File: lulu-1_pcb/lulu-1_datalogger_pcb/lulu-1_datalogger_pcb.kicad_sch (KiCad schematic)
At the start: 31 parts, among them J1 SD_Card_Receptacle, J3 USB_C_Receptacle_USB2.0_16P, J4 Conn_01x20_Socket, J5 Screw_Terminal_01x03, SW1 SW_Nidec_CAS-120A1, U1 STM32F401RETx, U2 BMP280, U3 MPU-6050, U4 W25Q16JVSS, U5 BD33FC0FP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

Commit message: deleted project
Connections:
- net GND: now also SW1.3 (A); no longer SW1.2 (B)
- net at R5.1: now also SW1.2 (B); no longer SW1.3 (A)
- no-connect marks 53 -> 51
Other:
- moved on the sheet: R5, SW1
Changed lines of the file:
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@@
 	)
 	(no_connect
-		(at 264.16 26.67)
-	)
-	(no_connect
 		(at 168.91 134.62)
 	)
@@
 	)
 	(no_connect
-		(at 218.44 39.37)
-	)
-	(no_connect
 		(at 168.91 129.54)
 	)
@@
 	(wire
 		(pts
+			(xy 113.03 60.96) (xy 115.57 60.96)
+		)
+		(stroke
+			(width 0)
+			(type default)
+		)
+	)
+	(wire
+		(pts
 			(xy 254 29.21) (xy 254 30.48)
 		)
@@
 	(wire
 		(pts
-			(xy 111.76 67.31) (xy 111.76 66.04)
-		)
-		(stroke
-			(width 0)
-			(type default)
-		)
-	)
-	(wire
-		(pts
 			(xy 254 91.44) (xy 250.19 91.44)
 		)
@@
 	(wire
 		(pts
+			(xy 254 26.67) (xy 264.16 26.67)
+		)
+		(stroke
+			(width 0)
+			(type default)
+		)
+	)
+	(wire
+		(pts
 			(xy 209.55 46.99) (xy 209.55 49.53)
 		)
@@
 	(wire
 		(pts
+			(xy 133.35 63.5) (xy 135.89 63.5)
+		)
+		(stroke
+			(width 0)
+			(type default)
+		)
+	)
+	(wire
+		(pts
 			(xy 43.18 90.17) (xy 45.72 90.17)
 		)
@@
 	(wire
 		(pts
-			(xy 125.73 68.58) (xy 123.19 68.58)
-		)
-		(stroke
-			(width 0)
-			(type default)
-		)
-	)
-	(wire
-		(pts
 			(xy 104.14 76.2) (xy 104.14 78.74)
 		)
@@
 	(wire
 		(pts
+			(xy 111.76 66.04) (xy 115.57 66.04)
+		)
+		(stroke
+			(width 0)
+			(type default)
+		)
+	)
+	(wire
+		(pts
 			(xy 78.74 119.38) (xy 82.55 119.38)
 		)
@@
 	(wire
 		(pts
-			(xy 135.89 63.5) (xy 130.81 63.5)
+			(xy 43.18 80.01) (xy 46.99 80.01)
 		)
 		(stroke
@@
 	(wire
 		(pts
-			(xy 43.18 80.01) (xy 46.99 80.01)
+			(xy 212.09 39.37) (xy 218.44 39.37)
 		)
 		(stroke
@@
 	(wire
 		(pts
-			(xy 111.76 66.04) (xy 113.03 66.04)
-		)
-		(stroke
-			(width 0)
-			(type default)
-		)
-	)
-	(wire
-		(pts
 			(xy 264.16 31.75) (xy 256.54 31.75)
 		)
@@
 	(symbol
 		(lib_id "Switch:SW_Nidec_CAS-120A1")
-		(at 118.11 66.04 0)
+		(at 120.65 63.5 180)
 		(unit 1)
 		(exclude_from_sim no)
@@
 		(on_board yes)
 		(dnp no)
-		(fields_autoplaced yes)
 		(property "Reference" "SW1"
-			(at 118.11 59.69 0)
+			(at 120.396 58.674 0)
 			(effects
 				(font
@@
 		)
 		(property "Value" "SW_Nidec_CAS-120A1"
-			(at 118.11 59.69 0)
+			(at 120.65 69.85 0)
 			(effects
 				(font
@@
 		)
 		(property "Footprint" "Button_Switch_SMD:Nidec_Copal_CAS-120A"
-			(at 118.11 76.2 0)
+			(at 120.65 53.34 0)
 			(effects
 				(font
@@
 		)
 		(property "Datasheet" "https://www.nidec-components.com/e/catalog/switch/cas.pdf"
-			(at 118.11 73.66 0)
+			(at 120.65 55.88 0)
 			(effects
 				(font
@@
 		)
 		(property "Description" "Switch, single pole double throw"
-			(at 118.11 66.04 0)
+			(at 120.65 63.5 0)
 			(effects
 				(font
@@
 	(symbol
 		(lib_id "Device:R")
-		(at 127 63.5 90)
+		(at 129.54 63.5 90)
 		(unit 1)
 		(exclude_from_sim no)
@@
 		(dnp no)
 		(property "Reference" "R5"
-			(at 126.492 58.928 90)
+			(at 129.032 58.928 90)
 			(effects
 				(font
@@
 		)
 		(property "Value" "10k"
-			(at 126.746 61.214 90)
+			(at 129.286 61.214 90)
 			(effects
 				(font
@@
 		)
 		(property "Footprint" ""
-			(at 127 65.278 90)
+			(at 129.54 65.278 90)
 			(effects
 				(font
@@
 		)
 		(property "Datasheet" "~"
-			(at 127 63.5 0)
+			(at 129.54 63.5 0)
 			(effects
 				(font
@@
 		)
 		(property "Description" "Resistor"
-			(at 127 63.5 0)
+			(at 129.54 63.5 0)
 			(effects
 				(font
@@
 	(symbol
 		(lib_id "power:VDD")
-		(at 125.73 68.58 270)
+		(at 113.03 60.96 90)
 		(unit 1)
 		(exclude_from_sim no)
@@
 		(dnp no)
 		(property "Reference" "#PWR018"
-			(at 121.92 68.58 0)
+			(at 116.84 60.96 0)
 			(effects
 				(font
@@
 		)
 		(property "Value" "+3.3V"
-			(at 126.492 71.12 90)
+			(at 115.57 58.928 90)
 			(effects
 				(font
@@
 		)
 		(property "Footprint" ""
-			(at 125.73 68.58 0)
+			(at 113.03 60.96 0)
 			(effects
 				(font
@@
 		)
 		(property "Datasheet" ""
-			(at 125.73 68.58 0)
+			(at 113.03 60.96 0)
 			(effects
 				(font
@@
 		)
 		(property "Description" "Power symbol creates a global label with name \"VDD\""
-			(at 125.73 68.58 0)
+			(at 113.03 60.96 0)
 			(effects
 				(font
@@
 	(symbol
 		(lib_id "power:GND")
-		(at 111.76 67.31 0)
+		(at 111.76 66.04 0)
 		(unit 1)
 		(exclude_from_sim no)
@@
 		(dnp no)
 		(property "Reference" "#PWR019"
-			(at 111.76 73.66 0)
+			(at 111.76 72.39 0)
 			(effects
 				(font
@@
 		)
 		(property "Value" "GND"
-			(at 111.76 71.12 0)
+			(at 111.76 69.85 0)
 			(effects
 				(font
@@
 		)
 		(property "Footprint" ""
-			(at 111.76 67.31 0)
+			(at 111.76 66.04 0)
 			(effects
 				(font
@@
 		)
 		(property "Datasheet" ""
-			(at 111.76 67.31 0)
+			(at 111.76 66.04 0)
 			(effects
 				(font
@@
 		)
 		(property "Description" "Power symbol creates a global label with name \"GND\" , ground"
-			(at 111.76 67.31 0)
+			(at 111.76 66.04 0)
 			(effects
 				(font

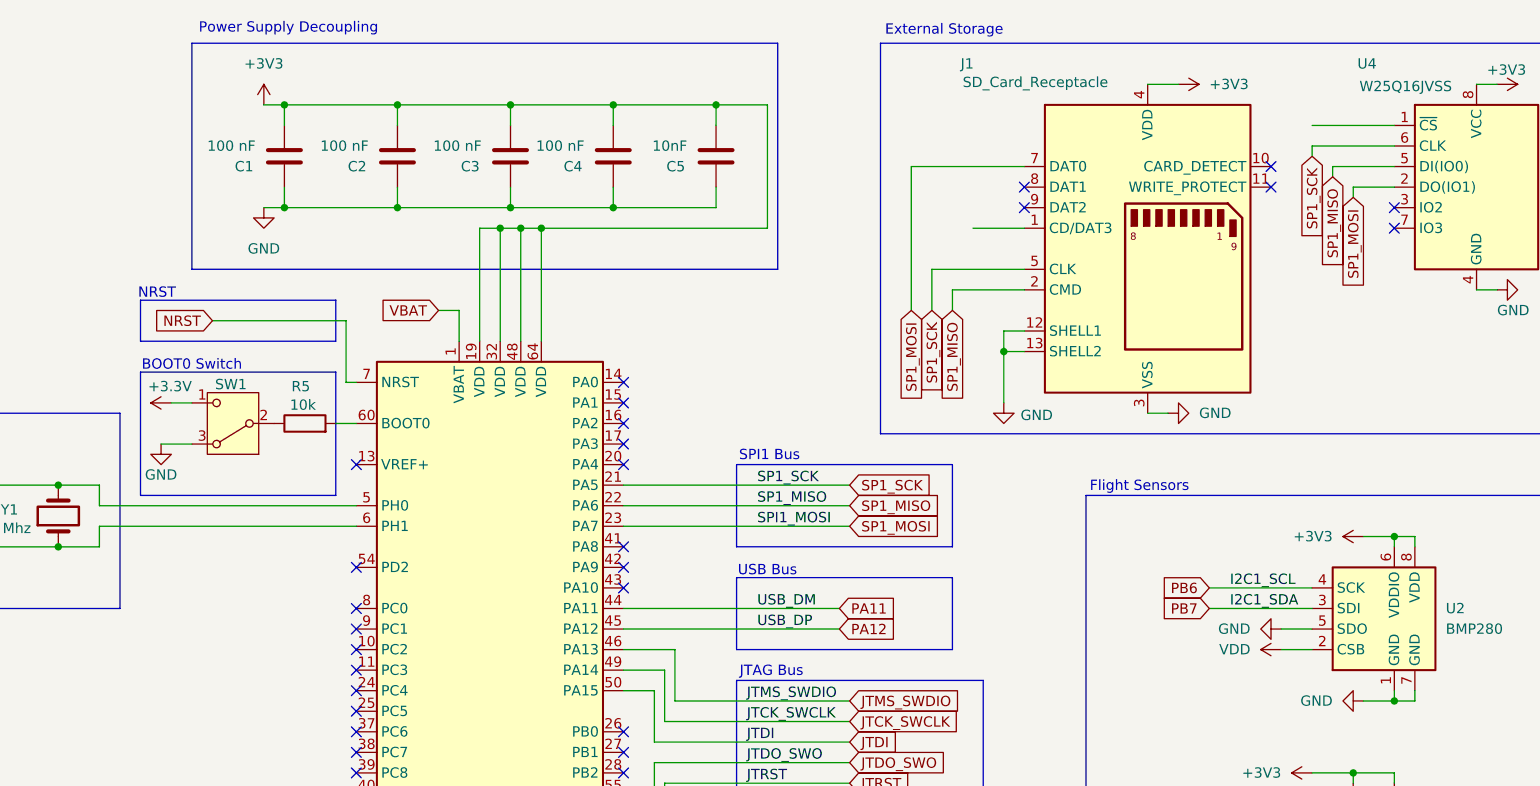
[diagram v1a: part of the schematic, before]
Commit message: initialised pins for SPI CS and added on schematic
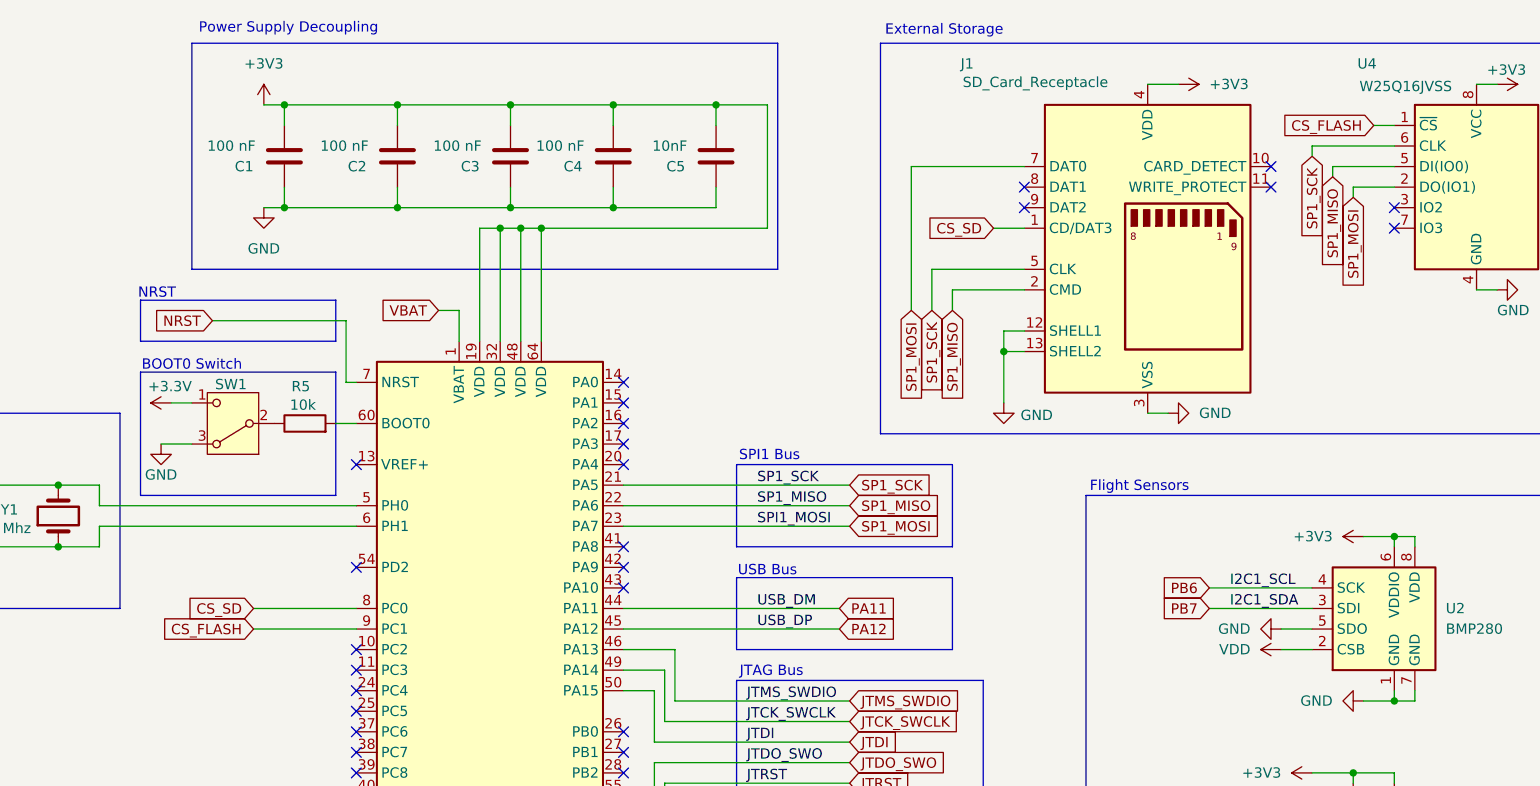
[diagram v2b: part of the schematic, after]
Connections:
- net CS_SD: now reaches J1.1 (CD/DAT3)
- net CS_SD: now also U1.8 (PC0)
- net CS_FLASH: now reaches U4.1 (~{CS})
- net CS_FLASH: now also U1.9 (PC1)
- no-connect marks 51 -> 49
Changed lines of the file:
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@@
 	)
 	(no_connect
-		(at 135.89 86.36)
-	)
-	(no_connect
 		(at 135.89 116.84)
 	)
@@
 	)
 	(no_connect
-		(at 135.89 88.9)
-	)
-	(no_connect
 		(at 135.89 99.06)
 	)
@@
 	(wire
 		(pts
+			(xy 123.19 86.36) (xy 135.89 86.36)
+		)
+		(stroke
+			(width 0)
+			(type default)
+		)
+	)
+	(wire
+		(pts
 			(xy 158.75 39.37) (xy 158.75 53.34)
 		)
@@
 	(wire
 		(pts
-			(xy 254 26.67) (xy 264.16 26.67)
+			(xy 123.19 88.9) (xy 135.89 88.9)
 		)
 		(stroke
@@
 	(wire
 		(pts
+			(xy 214.63 39.37) (xy 218.44 39.37)
+		)
+		(stroke
+			(width 0)
+			(type default)
+		)
+	)
+	(wire
+		(pts
 			(xy 33.02 186.69) (xy 33.02 187.96)
 		)
@@
 	(wire
 		(pts
+			(xy 261.62 26.67) (xy 264.16 26.67)
+		)
+		(stroke
+			(width 0)
+			(type default)
+		)
+	)
+	(wire
+		(pts
 			(xy 36.83 29.21) (xy 36.83 31.75)
 		)
@@
 	(wire
 		(pts
-			(xy 212.09 39.37) (xy 218.44 39.37)
-		)
-		(stroke
-			(width 0)
-			(type default)
-		)
-	)
-	(wire
-		(pts
 			(xy 187.96 134.62) (xy 187.96 135.89)
 		)
@@
 		)
 	)
+	(global_label "CS_SD"
+		(shape input)
+		(at 214.63 39.37 180)
+		(fields_autoplaced yes)
+		(effects
+			(font
+				(size 1.27 1.27)
+			)
+			(justify right)
+		)
+		(property "Intersheetrefs" "${INTERSHEET_REFS}"
+			(at 205.7182 39.37 0)
+			(effects
+				(font
+					(size 1.27 1.27)
+				)
+				(justify right)
+				(hide yes)
+			)
+		)
+	)
 	(global_label "SP1_MOSI"
 		(shape input)
@@
 		)
 	)
+	(global_label "CS_SD"
+		(shape input)
+		(at 123.19 86.36 180)
+		(fields_autoplaced yes)
+		(effects
+			(font
+				(size 1.27 1.27)
+			)
+			(justify right)
+		)
+		(property "Intersheetrefs" "${INTERSHEET_REFS}"
+			(at 114.2782 86.36 0)
+			(effects
+				(font
+					(size 1.27 1.27)
+				)
+				(justify right)
+				(hide yes)
+			)
+		)
+	)
 	(global_label "VBAT"
 		(shape input)
@@
 		)
 	)
+	(global_label "CS_FLASH"
+		(shape input)
+		(at 261.62 26.67 180)
+		(fields_autoplaced yes)
+		(effects
+			(font
+				(size 1.27 1.27)
+			)
+			(justify right)
+		)
+		(property "Intersheetrefs" "${INTERSHEET_REFS}"
+			(at 249.4424 26.67 0)
+			(effects
+				(font
+					(size 1.27 1.27)
+				)
+				(justify right)
+				(hide yes)
+			)
+		)
+	)
 	(global_label "JTDO_SWO"
 		(shape input)
@@
 			(effects
 				(font
+					(size 1.27 1.27)
+				)
+				(justify right)
+				(hide yes)
+			)
+		)
+	)
+	(global_label "CS_FLASH"
+		(shape input)
+		(at 123.19 88.9 180)
+		(fields_autoplaced yes)
+		(effects
+			(font
+				(size 1.27 1.27)
+			)
+			(justify right)
+		)
+		(property "Intersheetrefs" "${INTERSHEET_REFS}"
+			(at 111.0124 88.9 0)
+			(effects
+				(font

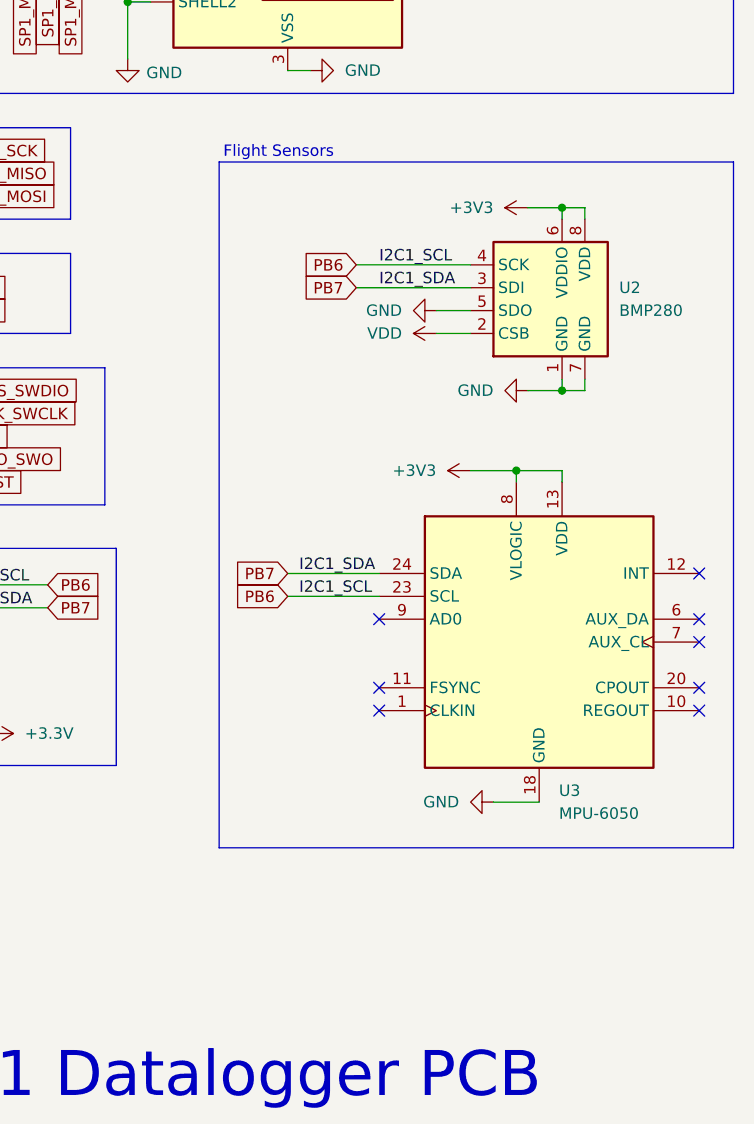
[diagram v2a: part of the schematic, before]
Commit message: decoupling capactirs to i2c components as per datasheets
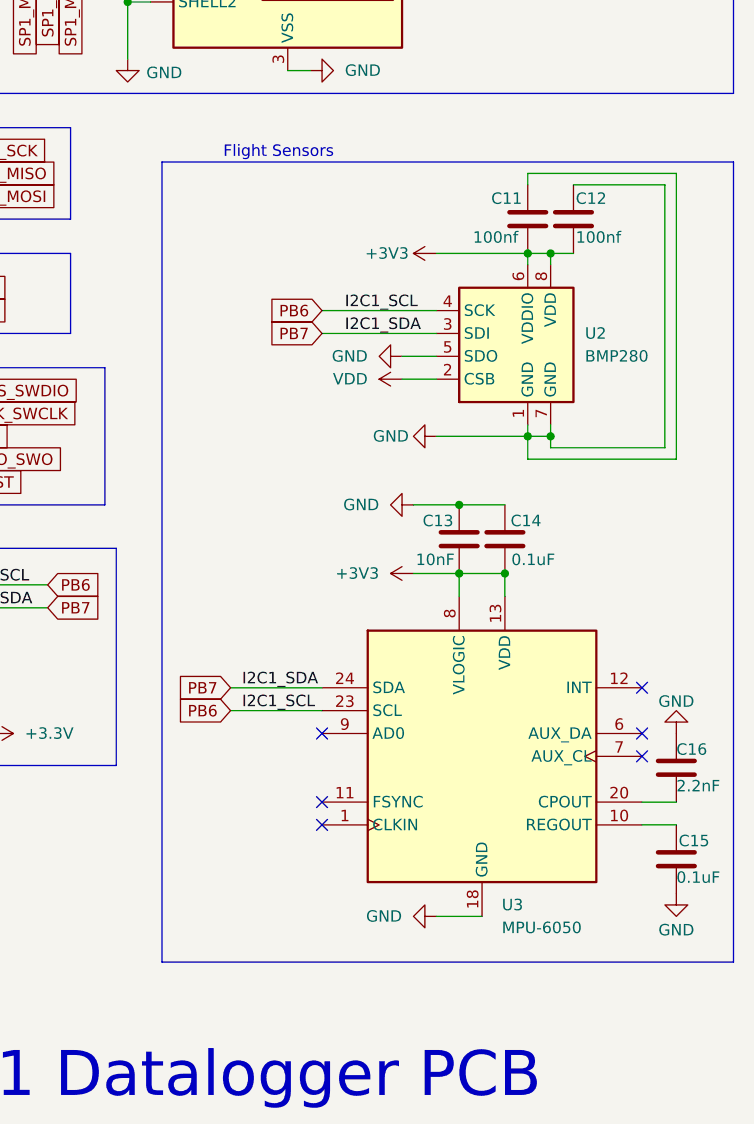
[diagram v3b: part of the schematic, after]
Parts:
- added C11, C12: 100nf, symbol Device:C
- added C13: 10nF, symbol Device:C
- added C14, C15: 0.1uF, symbol Device:C
- added C16: 2.2nF, symbol Device:C
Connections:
- net +3V3: now also C11.2, C12.2, C13.2, C14.1
- net GND: now also C11.1, C12.1, C13.1, C14.2, C15.2, C16.1
- net at U3.10 (REGOUT): now also C15.1
- net at U3.20 (CPOUT): now also C16.2
- no-connect marks 49 -> 47
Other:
- moved on the sheet: U2, U3
